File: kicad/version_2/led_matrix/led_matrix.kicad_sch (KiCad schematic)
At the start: 37 parts, among them Q1 IRF540N, Q2 IRF540N, Q3 IRF540N, Q4 IRF540N, Q5 IRF540N, Q6 IRF540N, Q7 IRF540N, Q9 IRF540N, SW1 SW_DIP_x01

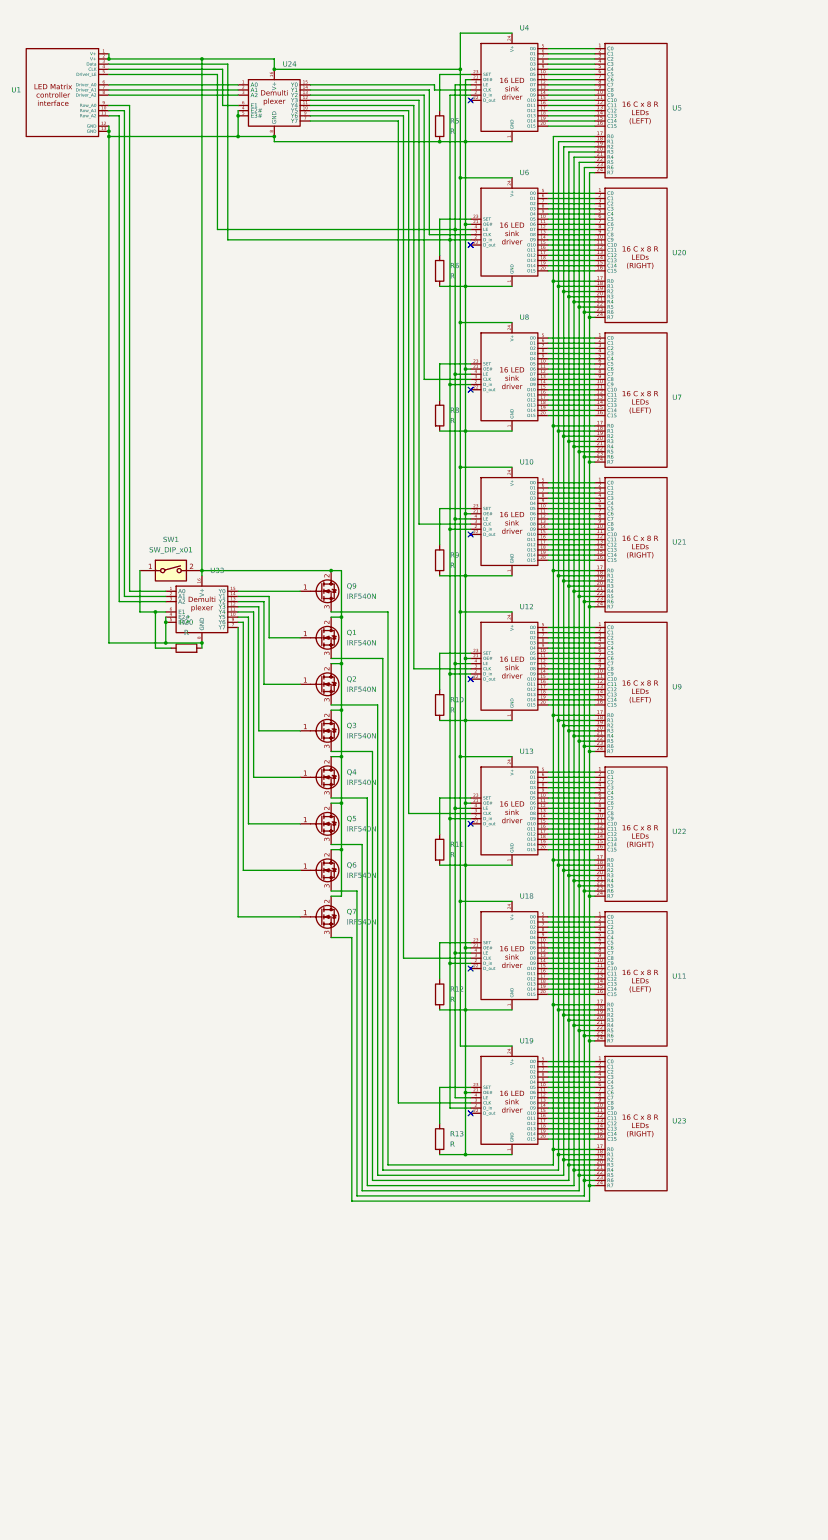
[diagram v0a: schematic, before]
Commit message: Added new led matrix board for the 8x8 displays
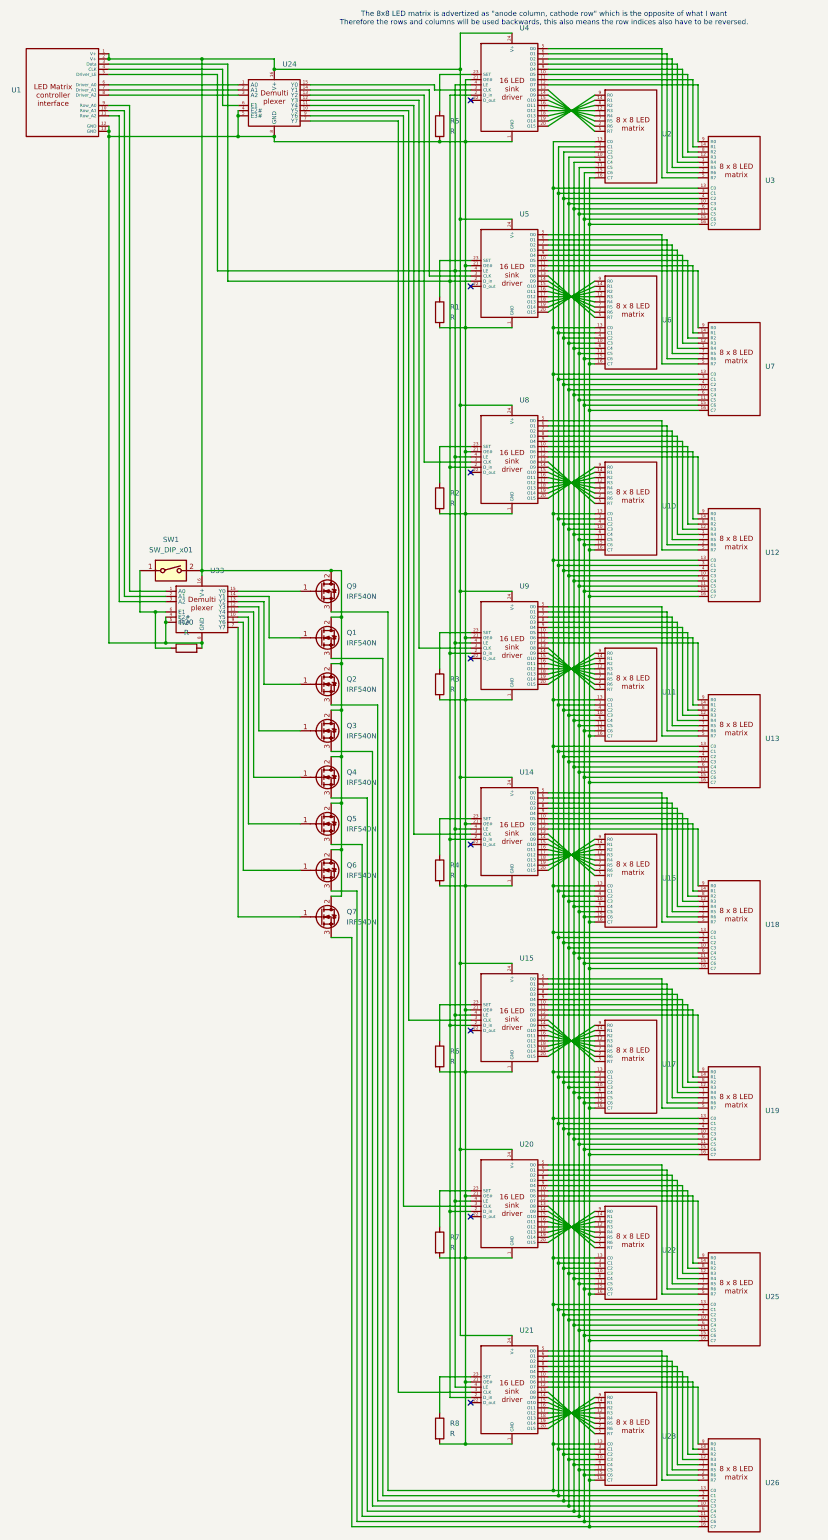
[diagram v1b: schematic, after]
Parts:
- removed R10, R11, R12, R13, R9: R, custom_footprint_library:0.4_pitch_resistor, symbol Device:R
- removed U10, U12, U13, U18, U19, U6: ~, Package_DIP:DIP-24_W7.62mm, symbol custom_symbol_lib:led_sink_16_bit
- removed U11, U5, U7, U9: ~, custom_footprint_library:led_block_16_x_8_left, symbol custom_symbol_lib:led_block_16_x_8_left
- removed U20, U21, U22, U23: ~, custom_footprint_library:led_block_16_x_8_right, symbol custom_symbol_lib:led_block_16_x_8_right
- added R1, R2, R3, R4, R7: R, custom_footprint_library:0.4_pitch_resistor, symbol Device:R
- added U10, U11, U12, U13, U16, U17, U18, U19, U2, U22, U23, U25, U26, U3, U6, U7: ~, custom_footprint_library:8_x_8_led_matrix_KWM-30881CVB, symbol custom_symbol_lib:led_matrix_adafruit_8_x_8
- added U14, U15, U20, U21, U5, U9: ~, Package_DIP:DIP-24_W7.62mm, symbol custom_symbol_lib:led_sink_16_bit
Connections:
- net at R20.2, R5.2, R6.2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: now also R1.2, R2.2, R3.2, R4.2, R7.2, U14.1 (GND), U14.21 (OE#), U15.1 (GND), U15.21 (OE#), U20.1 (GND), U20.21 (OE#), U21.1 (GND), U21.21 (OE#), U5.1 (GND), U5.21 (OE#), U9.1 (GND), U9.21 (OE#)
- net at U1.3 (Data), U4.2 (D_in), U8.2 (D_in): now also U14.2 (D_in), U15.2 (D_in), U20.2 (D_in), U21.2 (D_in), U5.2 (D_in), U9.2 (D_in)
- net at Q1.2 (D), Q2.2 (D), Q3.2 (D)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: now also U14.24 (V+), U15.24 (V+), U20.24 (V+), U21.24 (V+), U5.24 (V+), U9.24 (V+)
- net at U24.10 (Y5): now also U15.3 (CLK)
- net at U1.5 (Driver_LE), U4.4 (LE), U8.4 (LE): now also U14.4 (LE), U15.4 (LE), U20.4 (LE), U21.4 (LE), U5.4 (LE), U9.4 (LE)
- net at U24.11 (Y4): now also U14.3 (CLK)
- net at U24.12 (Y3): now also U9.3 (CLK)
- net at U24.14 (Y1): now also U5.3 (CLK)
- net at U24.7 (Y7): now also U21.3 (CLK)
- net at U24.9 (Y6): now also U20.3 (CLK)
- net at Q1.3 (S): now also U10.3 (C1), U11.3 (C1), U12.3 (C1), U13.3 (C1), U16.3 (C1), U17.3 (C1), U18.3 (C1), U19.3 (C1), U2.3 (C1), U22.3 (C1), U23.3 (C1), U25.3 (C1), U26.3 (C1), U3.3 (C1), U6.3 (C1), U7.3 (C1)
- net at Q5.3 (S): now also U10.11 (C5), U11.11 (C5), U12.11 (C5), U13.11 (C5), U16.11 (C5), U17.11 (C5), U18.11 (C5), U19.11 (C5), U2.11 (C5), U22.11 (C5), U23.11 (C5), U25.11 (C5), U26.11 (C5), U3.11 (C5), U6.11 (C5), U7.11 (C5)
- net at Q2.3 (S): now also U10.4 (C2), U11.4 (C2), U12.4 (C2), U13.4 (C2), U16.4 (C2), U17.4 (C2), U18.4 (C2), U19.4 (C2), U2.4 (C2), U22.4 (C2), U23.4 (C2), U25.4 (C2), U26.4 (C2), U3.4 (C2), U6.4 (C2), U7.4 (C2)
- net at Q3.3 (S): now also U10.10 (C3), U11.10 (C3), U12.10 (C3), U13.10 (C3), U16.10 (C3), U17.10 (C3), U18.10 (C3), U19.10 (C3), U2.10 (C3), U22.10 (C3), U23.10 (C3), U25.10 (C3), U26.10 (C3), U3.10 (C3), U6.10 (C3), U7.10 (C3)
- net at Q9.3 (S): now also U10.13 (C0), U11.13 (C0), U12.13 (C0), U13.13 (C0), U16.13 (C0), U17.13 (C0), U18.13 (C0), U19.13 (C0), U2.13 (C0), U22.13 (C0), U23.13 (C0), U25.13 (C0), U26.13 (C0), U3.13 (C0), U6.13 (C0), U7.13 (C0)
- net at Q4.3 (S): now also U10.6 (C4), U11.6 (C4), U12.6 (C4), U13.6 (C4), U16.6 (C4), U17.6 (C4), U18.6 (C4), U19.6 (C4), U2.6 (C4), U22.6 (C4), U23.6 (C4), U25.6 (C4), U26.6 (C4), U3.6 (C4), U6.6 (C4), U7.6 (C4)
- net at Q6.3 (S): now also U10.15 (C6), U11.15 (C6), U12.15 (C6), U13.15 (C6), U16.15 (C6), U17.15 (C6), U18.15 (C6), U19.15 (C6), U2.15 (C6), U22.15 (C6), U23.15 (C6), U25.15 (C6), U26.15 (C6), U3.15 (C6), U6.15 (C6), U7.15 (C6)
- net at Q7.3 (S): now also U10.16 (C7), U11.16 (C7), U12.16 (C7), U13.16 (C7), U16.16 (C7), U17.16 (C7), U18.16 (C7), U19.16 (C7), U2.16 (C7), U22.16 (C7), U23.16 (C7), U25.16 (C7), U26.16 (C7), U3.16 (C7), U6.16 (C7), U7.16 (C7)
- net at R6.1: now also U15.23 (SET)
- net at R8.1: now also U21.23 (SET); no longer U8.23 (SET)
- net at U8.10 (O5): now also U12.8 (R2)
- net at U8.11 (O6): now also U12.14 (R1)
- net at U8.12 (O7): now also U12.9 (R0)
- net at U8.13 (O8): now also U10.5 (R7)
- net at U8.14 (O9): now also U10.2 (R6)
- net at U8.15 (O10): now also U10.7 (R5)
- net at U8.16 (O11): now also U10.1 (R4)
- net at U8.17 (O12): now also U10.12 (R3)
- net at U8.18 (O13): now also U10.8 (R2)
- net at U8.19 (O14): now also U10.14 (R1)
- net at U8.20 (O15): now also U10.9 (R0)
- net at U8.5 (O0): now also U12.5 (R7)
- net at U8.6 (O1): now also U12.2 (R6)
- net at U8.7 (O2): now also U12.7 (R5)
- net at U8.8 (O3): now also U12.1 (R4)
- net at U8.9 (O4): now also U12.12 (R3)
- net at U4.5 (O0): now also U3.5 (R7)
- net at U4.14 (O9): now also U2.2 (R6)
- net at U4.15 (O10): now also U2.7 (R5)
- net at U4.16 (O11): now also U2.1 (R4)
- net at U4.17 (O12): now also U2.12 (R3)
- net at U4.18 (O13): now also U2.8 (R2)
- net at U4.19 (O14): now also U2.14 (R1)
- net at U4.20 (O15): now also U2.9 (R0)
- net at U4.6 (O1): now also U3.2 (R6)
- net at U4.7 (O2): now also U3.7 (R5)
- net at U4.8 (O3): now also U3.1 (R4)
- net at U4.9 (O4): now also U3.12 (R3)
- net at U4.10 (O5): now also U3.8 (R2)
- net at U4.11 (O6): now also U3.14 (R1)
- net at U4.12 (O7): now also U3.9 (R0)
- net at U4.13 (O8): now also U2.5 (R7)
- new net: U20.8 (O3), U25.1 (R4)
- new net: U20.9 (O4), U25.12 (R3)
- new net: U20.11 (O6), U25.14 (R1)
- new net: U20.6 (O1), U25.2 (R6)
- new net: U20.5 (O0), U25.5 (R7)
- new net: U20.7 (O2), U25.7 (R5)
- new net: U20.10 (O5), U25.8 (R2)
- new net: U20.12 (O7), U25.9 (R0)
- new net: U5.16 (O11), U6.1 (R4)
- new net: U5.17 (O12), U6.12 (R3)
- new net: U5.19 (O14), U6.14 (R1)
- new net: U5.14 (O9), U6.2 (R6)
- new net: U5.13 (O8), U6.5 (R7)
- new net: U5.15 (O10), U6.7 (R5)
- new net: U5.18 (O13), U6.8 (R2)
- new net: U5.20 (O15), U6.9 (R0)
- new net: U11.1 (R4), U9.16 (O11)
- new net: U11.12 (R3), U9.17 (O12)
- new net: U11.14 (R1), U9.19 (O14)
- new net: U11.2 (R6), U9.14 (O9)
- new net: U11.5 (R7), U9.13 (O8)
- new net: U11.7 (R5), U9.15 (O10)
- new net: U11.8 (R2), U9.18 (O13)
- new net: U11.9 (R0), U9.20 (O15)
- new net: U15.16 (O11), U17.1 (R4)
- new net: U15.17 (O12), U17.12 (R3)
- new net: U15.19 (O14), U17.14 (R1)
- new net: U15.14 (O9), U17.2 (R6)
- new net: U15.13 (O8), U17.5 (R7)
- new net: U15.15 (O10), U17.7 (R5)
- new net: U15.18 (O13), U17.8 (R2)
- new net: U15.20 (O15), U17.9 (R0)
- new net: U21.10 (O5), U26.8 (R2)
- new net: U21.11 (O6), U26.14 (R1)
- new net: U21.12 (O7), U26.9 (R0)
- new net: U21.13 (O8), U23.5 (R7)
- new net: U21.14 (O9), U23.2 (R6)
- new net: U21.15 (O10), U23.7 (R5)
- new net: U21.16 (O11), U23.1 (R4)
- new net: U21.17 (O12), U23.12 (R3)
- new net: U21.18 (O13), U23.8 (R2)
- new net: U21.19 (O14), U23.14 (R1)
- new net: U21.20 (O15), U23.9 (R0)
- new net: U21.5 (O0), U26.5 (R7)
- new net: U21.6 (O1), U26.2 (R6)
- new net: U21.7 (O2), U26.7 (R5)
- new net: U21.8 (O3), U26.1 (R4)
- new net: U21.9 (O4), U26.12 (R3)
- new net: R3.1, U9.23 (SET)
- new net: U20.13 (O8), U22.5 (R7)
- new net: U20.14 (O9), U22.2 (R6)
- new net: U20.15 (O10), U22.7 (R5)
- new net: U20.16 (O11), U22.1 (R4)
- new net: U20.17 (O12), U22.12 (R3)
- new net: U20.18 (O13), U22.8 (R2)
- new net: U20.19 (O14), U22.14 (R1)
- new net: U20.20 (O15), U22.9 (R0)
- new net: R7.1, U20.23 (SET)
- new net: U14.16 (O11), U16.1 (R4)
- new net: U14.17 (O12), U16.12 (R3)
- new net: U14.19 (O14), U16.14 (R1)
- new net: U14.14 (O9), U16.2 (R6)
- new net: U14.13 (O8), U16.5 (R7)
- new net: U14.15 (O10), U16.7 (R5)
- new net: U14.18 (O13), U16.8 (R2)
- new net: U14.20 (O15), U16.9 (R0)
- new net: U14.10 (O5), U18.8 (R2)
- new net: U14.11 (O6), U18.14 (R1)
- new net: U14.12 (O7), U18.9 (R0)
- new net: R4.1, U14.23 (SET)
- new net: U14.5 (O0), U18.5 (R7)
- new net: U14.6 (O1), U18.2 (R6)
- new net: U14.7 (O2), U18.7 (R5)
- new net: U14.8 (O3), U18.1 (R4)
- new net: U14.9 (O4), U18.12 (R3)
- new net: U5.8 (O3), U7.1 (R4)
- new net: U5.9 (O4), U7.12 (R3)
- new net: U5.11 (O6), U7.14 (R1)
- new net: U5.6 (O1), U7.2 (R6)
- new net: U5.5 (O0), U7.5 (R7)
- new net: U5.7 (O2), U7.7 (R5)
- new net: U5.10 (O5), U7.8 (R2)
- new net: U5.12 (O7), U7.9 (R0)
- new net: R1.1, U5.23 (SET)
- new net: U13.8 (R2), U9.10 (O5)
- new net: U13.14 (R1), U9.11 (O6)
- new net: U13.9 (R0), U9.12 (O7)
- new net: U13.5 (R7), U9.5 (O0)
- new net: U13.2 (R6), U9.6 (O1)
- new net: U13.7 (R5), U9.7 (O2)
- new net: U13.1 (R4), U9.8 (O3)
- new net: U13.12 (R3), U9.9 (O4)
- new net: R2.1, U8.23 (SET)
- new net: U15.10 (O5), U19.8 (R2)
- new net: U15.11 (O6), U19.14 (R1)
- new net: U15.12 (O7), U19.9 (R0)
- new net: U15.5 (O0), U19.5 (R7)
- new net: U15.6 (O1), U19.2 (R6)
- new net: U15.7 (O2), U19.7 (R5)
- new net: U15.8 (O3), U19.1 (R4)
- new net: U15.9 (O4), U19.12 (R3)
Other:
- note added: "The 8x8 LED matrix is advertized as "anode column, cathode row" which is the opposite of what I want Therefore the rows and columns will be used backwards, this also means the row indices also have to be reversed."
